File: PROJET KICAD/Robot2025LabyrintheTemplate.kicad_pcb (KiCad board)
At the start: 2 copper layers, 76.2 x 54.6 mm, 23 parts, among them J1 HC-SR04 gauche, J10 CAPTEUR TOF _BAS, J11 SERVO MOTEUR 4, J2 +VBatt, J3 SERVO MOTEUR 1, J4 SERVO MOTEUR 2, J5 cap sen0101, J7 SERVO MOTEUR 3, J8 HC-SR04 droite, J9 CAPTEUR TOF_HAUT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

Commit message: revue avec alaime
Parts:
- removed U3: NRF24L01P-Module-E01ML01DP5_Breakout, ISI-Modules:E01-ML01DP5
- added C3: C_Gen, ISI-Capacitor:C_1206_3216Metric_Pad1.33x1.80mm_HandSolder, F.Cu at (207.4, 138.0)
- added C4: C_Polarized, ISI-Capacitor:CP_EIA-6032-28_Kemet-C_Pad2.25x2.35mm_HandSolder, F.Cu at (272.9, 134.0)
- added J10: CAPTEUR TOF _BAS, ISI-Connector_PinHeader_2.54mm:PinHeader_1x06_P2.54mm_Long_Vertical, F.Cu at (209.3, 73.5)
- added J12: Conn_01x06_Pin, ISI-Connector_PinHeader_2.54mm:PinHeader_1x06_P2.54mm_Long_Vertical, F.Cu at (82.1, 34.5)
- added J13: Conn_01x06_Pin, ISI-Connector_PinHeader_2.54mm:PinHeader_1x06_P2.54mm_Long_Vertical, F.Cu at (212.9, 59.0)
- added J14: Conn_01x06_Pin, ISI-Connector_PinHeader_2.54mm:PinHeader_1x06_P2.54mm_Long_Vertical, F.Cu at (219.5, 129.4)
- added J14: Conn_01x02_Pin, ISI-Connector_JST:JST_XH_B2B-XH-AM_1x02_P2.50mm_Long_Vertical, F.Cu at (246.0, 116.0)
- added J15: CON 1x2 POLARIZED, ISI-Connector_Generic:AMASS_XT60-F_1x02_P7.20mm_Vertical, F.Cu at (64.4, 76.5)
- added J16: regulateur, ISI-Connector_JST:JST_XH_B2B-XH-AM_1x02_P2.50mm_Long_Vertical, F.Cu at (262.5, 127.2)
- added J17: Conn_01x04_Pin, ISI-Connector_JST:JST_XH_B4B-XH-AM_1x04_P2.50mm_Long_Vertical, F.Cu at (271.9, 119.4)
- added J18: Conn_01x02_Pin, ISI-Connector_JST:JST_XH_B2B-XH-AM_1x02_P2.50mm_Long_Vertical, F.Cu at (262.5, 135.0)
- added J19: Conn_01x04_Pin, ISI-Connector_JST:JST_XH_B4B-XH-AM_1x04_P2.50mm_Long_Vertical, F.Cu at (271.9, 127.2)
- added J6: Conn_01x06_Pin, ISI-Connector_PinHeader_2.54mm:PinHeader_1x06_P2.54mm_Long_Vertical, F.Cu at (83.1, 121.5)
- added J9: CAPTEUR TOF_HAUT, ISI-Connector_PinHeader_2.54mm:PinHeader_1x06_P2.54mm_Long_Vertical, F.Cu at (212.4, 99.5)
- added U2: LM1117MPX-3.3, ISI-IC:SOT-223-3_TabPin2, F.Cu at (173.2, 132.5)
- added U4: NRF24L01P-Module-E01ML01DP5_Breakout, ISI-Modules:E01-ML01DP5, F.Cu at (181.2, 145.1)
- C1, C2: value 10uF -> C_Gen; footprint ISI-Capacitor:WCAP-ATUL_18X35.5_DXL_ -> ISI-Capacitor:C_1206_3216Metric_Pad1.33x1.80mm_HandSolder
- moved U1 230.5 mm to (232.0, 85.2)
- moved A5 176.2 mm to (215.9, 122.5), turned to 90 degrees
- moved A4 176.0 mm to (210.9, 49.7), turned to 90 degrees
- moved J3 141.9 mm to (153.5, 32.0)
- moved J5 116.8 mm to (150.5, 148.0)
- moved A2 110.6 mm to (94.5, 121.5)
- moved C1 108.7 mm to (168.9, 123.0)
- moved C2 104.2 mm to (165.0, 140.5), turned to 180 degrees
- moved J10 102.2 mm to (134.9, 125.2)
- moved J11 102.2 mm to (125.6, 125.2)
- moved J4 102.2 mm to (116.3, 125.2)
- moved J7 102.2 mm to (120.9, 125.2)
- moved J8 102.2 mm to (140.7, 126.3)
- moved J9 102.2 mm to (130.2, 125.2)
- moved J2 95.7 mm to (91.2, 144.0), turned to 0 degrees
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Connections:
- A1 pad 3: unconnected-(A1-A2-Pad3) -> Net-(A1-A2)
- A1 pad 4: unconnected-(A1-A1-Pad4) -> Net-(A1-A1)
- A1 pad 5: unconnected-(A1-B1-Pad5) -> Net-(A1-B1)
- A1 pad 6: unconnected-(A1-B2-Pad6) -> Net-(A1-B2)
- A1 pad 7: unconnected-(A1-GND-Pad7) -> Net-(J12-Pin_6)
- A1 pad 8: unconnected-(A1-VMOT-Pad8) -> Net-(A1-VMOT)
- A2 pad 3V3: +3V3 -> unconnected-(A2-3.3V-Pad3V3)
- A2 pad D20: /T_SDA -> Net-(A2-D20/SDA)
- A2 pad D21: /T_SCL -> Net-(A2-D21/SCL)
- A2 pad SCL: /SCL_1 -> unconnected-(A2-PadSCL)
- A2 pad SDA: /SDA_1 -> unconnected-(A2-PadSDA)
- A2 pad VIN: /Vin -> unconnected-(A2-PadVIN)
- A3 pad 3: unconnected-(A3-A2-Pad3) -> Net-(A3-A2)
- A3 pad 4: unconnected-(A3-A1-Pad4) -> Net-(A3-A1)
- A3 pad 5: unconnected-(A3-B1-Pad5) -> Net-(A3-B1)
- A3 pad 6: unconnected-(A3-B2-Pad6) -> Net-(A3-B2)
- A3 pad 7: unconnected-(A3-GND-Pad7) -> Net-(J6-Pin_6)
- A3 pad 8: unconnected-(A3-VMOT-Pad8) -> Net-(A3-VMOT)
- A4 pad 3: unconnected-(A4-A2-Pad3) -> Net-(A4-A2)
- A4 pad 4: unconnected-(A4-A1-Pad4) -> Net-(A4-A1)
- A5 pad 3: unconnected-(A5-A2-Pad3) -> Net-(A5-A2)
- A5 pad 4: unconnected-(A5-A1-Pad4) -> Net-(A5-A1)
- A5 pad 5: unconnected-(A5-B1-Pad5) -> Net-(A5-B1)
- A5 pad 6: unconnected-(A5-B2-Pad6) -> Net-(A5-B2)
- A5 pad 7: unconnected-(A5-GND-Pad7) -> GND
- A5 pad 8: unconnected-(A5-VMOT-Pad8) -> /Vin
- C1 pad 1: +3V3 -> Net-(U2-VO)
- C2 pad 1: GND -> +5V
- U1 pad 3: /SCL_1 -> Net-(A2-D21/SCL)
- U1 pad 4: /SDA_1 -> Net-(A2-D20/SDA)
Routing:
- net (no net): track 286.5 -> 0.00 mm, vias 4 -> 0
- net +3V3: track 29.8 -> 0.00 mm, vias 1 -> 0
- net /Trig_G: track 16.4 -> 0.00 mm, vias 1 -> 0
- net /Echo_G: track 15.8 -> 0.00 mm
- net /Vin: track 14.5 -> 0.00 mm
- net Net-(D3-A): track 5.55 -> 0.00 mm
- net Net-(D3-K): track 5.52 -> 0.00 mm
- net Net-(D2-A): track 2.40 -> 0.00 mm
- net GND: track 1.90 -> 0.00 mm, vias 1 -> 0
- removed copper zone on F.Cu, net +5V
- removed copper zone on B.Cu, net GND
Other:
- board size 76.2 x 54.6 mm -> 215 x 90 mm
- board text removed: "+"
- board text removed: "-"
- board text removed: "Capteur Temp"
- board text removed: "HC-SR04"
- board text removed: "Power"
- board text removed: "Projet B3 labyrinthe 2025"
- board text removed: "RFID-RC522"
- board text removed: "Servomoteur N1"
- board text removed: "Sig"

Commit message: test2
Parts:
- moved U1 55.5 mm to (183.0, 59.3)
- moved J3 8.11 mm to (148.0, 37.9)
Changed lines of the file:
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@@
 	(footprint "ISI-Connector_PinHeader_2.54mm:PinHeader_1x03_P2.54mm_Long_Vertical"
 		(layer "F.Cu")
-		(at 153.5 31.96)
+		(at 148 37.92)
 		(descr "Through hole straight pin header, 1x03, 2.54mm pitch, single row")
 		(tags "Through hole pin header THT 1x03 2.54mm single row")
@@
 	(footprint "ISI-Modules:module_mpu6050"
 		(layer "F.Cu")
-		(at 232 85.24)
+		(at 183 59.28)
 		(descr "Module 6 DoF I2C basé sur un MPU6050 associant un accéléromètre 3 axes et un gyroscope 3 axes.")
 		(property "Reference" "U1"

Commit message: fin de la schematique, debut rotage
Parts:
- removed C3: C_Gen, ISI-Capacitor:C_1206_3216Metric_Pad1.33x1.80mm_HandSolder
- removed J10 (x2): CAPTEUR TOF _BAS, ISI-Connector_PinHeader_2.54mm:PinHeader_1x06_P2.54mm_Long_Vertical
- removed J12: Conn_01x06_Pin, ISI-Connector_PinHeader_2.54mm:PinHeader_1x06_P2.54mm_Long_Vertical
- removed the J14 at (219.5, 129.4)
- removed J19: Conn_01x04_Pin, ISI-Connector_JST:JST_XH_B4B-XH-AM_1x04_P2.50mm_Long_Vertical
- removed J5: cap sen0101, ISI-Connector_PinSocket_2.54mm:PinSocket_2x04_P2.54mm_Vertical
- removed J9 (x2): CAPTEUR TOF_HAUT, ISI-Connector_PinHeader_2.54mm:PinHeader_1x06_P2.54mm_Long_Vertical
- added F1: Fuse, ISI-Divers:Fuseholder_TR5_Littelfuse_No560_No460, F.Cu at (59.5, 88.0)
- added J20: moteur 3 DR, ISI-Connector_JST:JST_XH_B4B-XH-AM_1x04_P2.50mm_Long_Vertical, F.Cu at (61.5, 58.0)
- added J21: moteur 4 DR, ISI-Connector_JST:JST_XH_B4B-XH-AM_1x04_P2.50mm_Long_Vertical, F.Cu at (56.5, 127.0)
- added J22: moteur 1 AV, ISI-Connector_JST:JST_XH_B4B-XH-AM_1x04_P2.50mm_Long_Vertical, F.Cu at (228.0, 74.0)
- added R2: 10k, ISI-Resistor:R_1206_3216Metric_Pad1.30x1.75mm_HandSolder, F.Cu at (181.4, 56.5)
- added R3: 10k, ISI-Resistor:R_1206_3216Metric_Pad1.30x1.75mm_HandSolder, F.Cu at (181.9, 60.5)
- J13: value Conn_01x06_Pin -> capteur TOF BAS; footprint ISI-Connector_PinHeader_2.54mm:PinHeader_1x06_P2.54mm_Long_Vertical -> ISI-Connector_JST:JST_XH_B5B-XH-AM_1x05_P2.50mm_Long_Vertical
- J14: value Conn_01x02_Pin -> Vinput regul
- J16: value regulateur -> capteur TOF HAUT; footprint ISI-Connector_JST:JST_XH_B2B-XH-AM_1x02_P2.50mm_Long_Vertical -> ISI-Connector_JST:JST_XH_B5B-XH-AM_1x05_P2.50mm_Long_Vertical
- J17: value Conn_01x04_Pin -> moteur 2 AV
- J18: value Conn_01x02_Pin -> Vout regul
- J2: value +VBatt -> cap sen0101; footprint ISI-Connector_JST:JST_XH_B2B-XH-AM_1x02_P2.50mm_Long_Vertical -> ISI-Connector_JST:JST_XH_B4B-XH-AM_1x04_P2.50mm_Long_Vertical; moved to B.Cu
- J6: value Conn_01x06_Pin -> cap sen0101; footprint ISI-Connector_PinHeader_2.54mm:PinHeader_1x06_P2.54mm_Long_Vertical -> ISI-Connector_JST:JST_XH_B4B-XH-AM_1x04_P2.50mm_Long_Vertical; moved to B.Cu
- moved J18 157.7 mm to (105.0, 126.0)
- moved J14 153.3 mm to (93.0, 125.5)
- moved J4 106.3 mm to (222.5, 122.5)
- moved J2 86.7 mm to (119.5, 62.0), turned to 90 degrees
- moved J7 86.2 mm to (71.0, 54.9)
- moved S1 73.9 mm to (73.0, 89.5)
- moved J3 69.5 mm to (215.0, 56.5)
- moved D3 65.8 mm to (63.3, 97.5)
- moved J6 64.8 mm to (107.5, 61.5), turned to 90 degrees
- moved C4 62.0 mm to (211.6, 125.0)
- moved R1 59.2 mm to (71.0, 93.5)
- moved J11 51.1 mm to (74.5, 124.0)
- moved J16 47.8 mm to (228.0, 94.0)
- moved C2 46.8 mm to (211.0, 132.0)
- moved D2 46.8 mm to (74.0, 98.0)
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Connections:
- A1 pad 10: +5V -> GND
- A1 pad 11: +5V -> GND
- A1 pad 12: +5V -> GND
- A1 pad 7: Net-(J12-Pin_6) -> GND
- A1 pad 8: Net-(A1-VMOT) -> /Vin
- A3 pad 10: +5V -> GND
- A3 pad 11: +5V -> GND
- A3 pad 12: +5V -> GND
- A3 pad 7: Net-(J6-Pin_6) -> GND
- A3 pad 8: Net-(A3-VMOT) -> /Vin
- A4 pad 10: +5V -> GND
- A4 pad 11: +5V -> GND
- A4 pad 12: +5V -> GND
- A4 pad 5: unconnected-(A4-B1-Pad5) -> Net-(A4-B1)
- A4 pad 6: unconnected-(A4-B2-Pad6) -> Net-(A4-B2)
- A4 pad 7: unconnected-(A4-GND-Pad7) -> GND
- A4 pad 8: unconnected-(A4-VMOT-Pad8) -> /Vin
- J11 pad 2: unconnected-(J11-Pin_2-Pad2) -> +5V
- J13 pad 1: Net-(A4-VMOT) -> +5V
- J13 pad 2: Net-(A4-A1) -> GND
- J13 pad 3: Net-(A4-A2) -> Net-(A2-D21/SCL)
- J13 pad 4: Net-(A4-B1) -> Net-(A2-D20/SDA)
- J13 pad 5: Net-(A4-B2) -> /D_XSHUT_B
- J14 pad 1: unconnected-(J14-Pin_1-Pad1) -> /Vin
- J14 pad 2: unconnected-(J14-Pin_2-Pad2) -> GND
- J15 pad 1: unconnected-(J15-Pad1) -> Net-(F1-Pad1)
- J15 pad 2: unconnected-(J15-Pad2) -> GND
- J16 pad 1: unconnected-(J16-Pin_1-Pad1) -> +5V
- J16 pad 2: unconnected-(J16-Pin_2-Pad2) -> GND
- J17 pad 1: Net-(A5-B2) -> Net-(A5-A1)
- J17 pad 2: Net-(A5-B1) -> Net-(A5-A2)
- J17 pad 3: Net-(A5-A2) -> Net-(A5-B1)
- J17 pad 4: Net-(A5-A1) -> Net-(A5-B2)
- J2 pad 1: Net-(D3-A) -> GND
- J2 pad 2: GND -> /D_OUT
- J3 pad 2: unconnected-(J3-Pin_2-Pad2) -> +5V
- J4 pad 2: unconnected-(J4-Pin_2-Pad2) -> +5V
- J6 pad 1: Net-(A3-VMOT) -> /D_S0
- J6 pad 2: Net-(A3-A1) -> /D_S1
- J6 pad 3: Net-(A3-A2) -> /D_S2
- J6 pad 4: Net-(A3-B1) -> /D_S3
- J7 pad 2: unconnected-(J7-Pin_2-Pad2) -> +5V
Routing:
- net Net-(A2-D21/SCL): track 0.00 -> 37.6 mm
- net Net-(A1-A2): track 0.00 -> 24.6 mm
- net Net-(A3-A2): track 0.00 -> 23.5 mm
- net Net-(A5-A2): track 0.00 -> 22.7 mm
- net Net-(A4-A2): track 0.00 -> 21.4 mm
- net Net-(A2-D20/SDA): track 0.00 -> 16.9 mm
- net Net-(A3-B1): track 0.00 -> 12.1 mm
- net Net-(A3-B2): track 0.00 -> 12.1 mm
- net Net-(A3-A1): track 0.00 -> 11.1 mm
- net Net-(A1-A1): track 0.00 -> 9.18 mm
- net Net-(A5-B1): track 0.00 -> 8.98 mm
- net Net-(A5-B2): track 0.00 -> 8.96 mm
- net Net-(A1-B2): track 0.00 -> 8.17 mm
- net Net-(A1-B1): track 0.00 -> 8.16 mm
- net Net-(A5-A1): track 0.00 -> 7.96 mm
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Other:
- board size 215 x 90 mm -> 210 x 85 mm

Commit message: routage 1
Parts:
- moved U1 85.3 mm to (123.0, 76.0), turned to -90 degrees
- moved J8 38.5 mm to (161.5, 88.0)
- moved J18 31.8 mm to (109.5, 94.5)
- moved J14 31.3 mm to (97.5, 94.5)
- moved J1 13.0 mm to (161.5, 101.5)
- moved S1 11.6 mm to (84.5, 89.0)
- moved R1 11.0 mm to (82.0, 93.0)
- moved D2 9.51 mm to (83.5, 97.5)
- moved D3 9.00 mm to (72.3, 97.5)
- moved C4 8.16 mm to (204.8, 120.3)
- moved C1 8.16 mm to (204.8, 114.3)
- moved C2 8.16 mm to (204.3, 127.3)
- moved F1 7.57 mm to (66.9, 89.5)
- moved U2 7.29 mm to (196.0, 120.7)
- moved U4 5.06 mm to (192.3, 110.0)
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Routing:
- net Net-(A2-D21/SCL): track 37.6 -> 16.2 mm
- net Net-(A2-D20/SDA): track 16.9 -> 19.1 mm
- net Net-(A3-A1): track 11.1 -> 9.76 mm

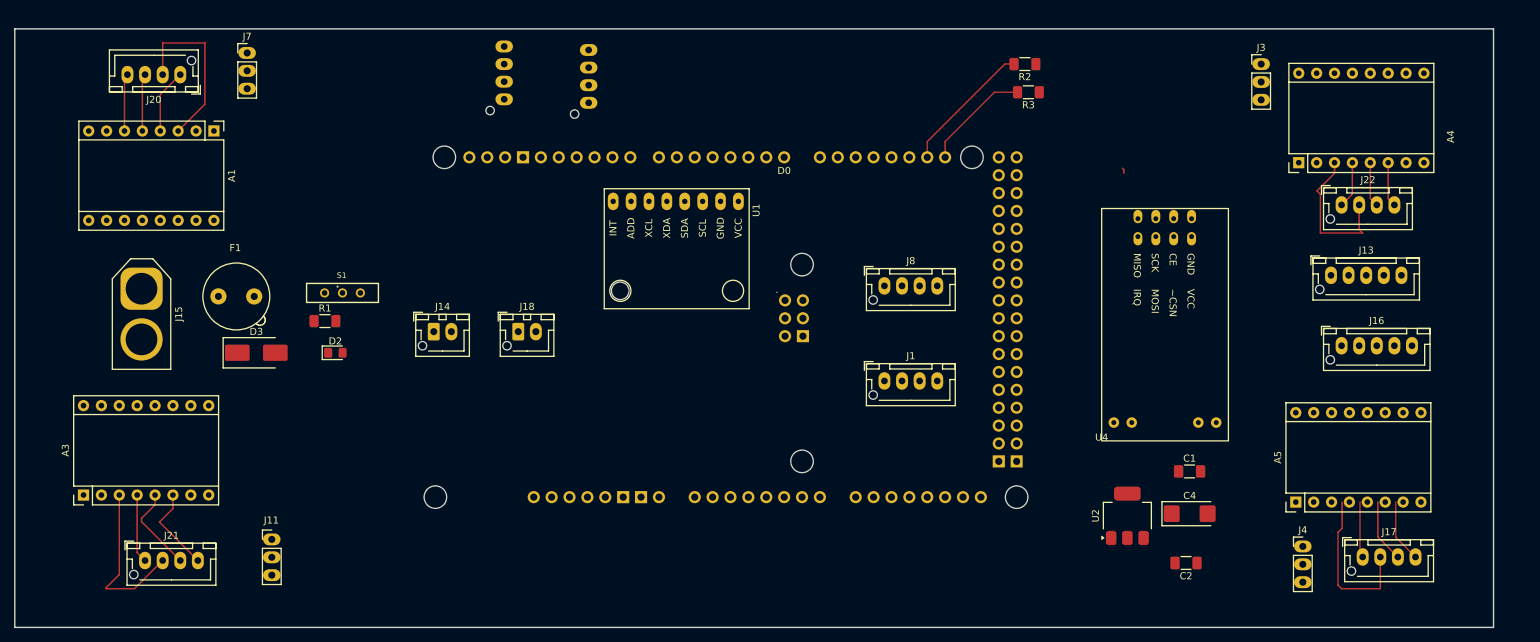
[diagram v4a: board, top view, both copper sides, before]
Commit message: gnd et 5v
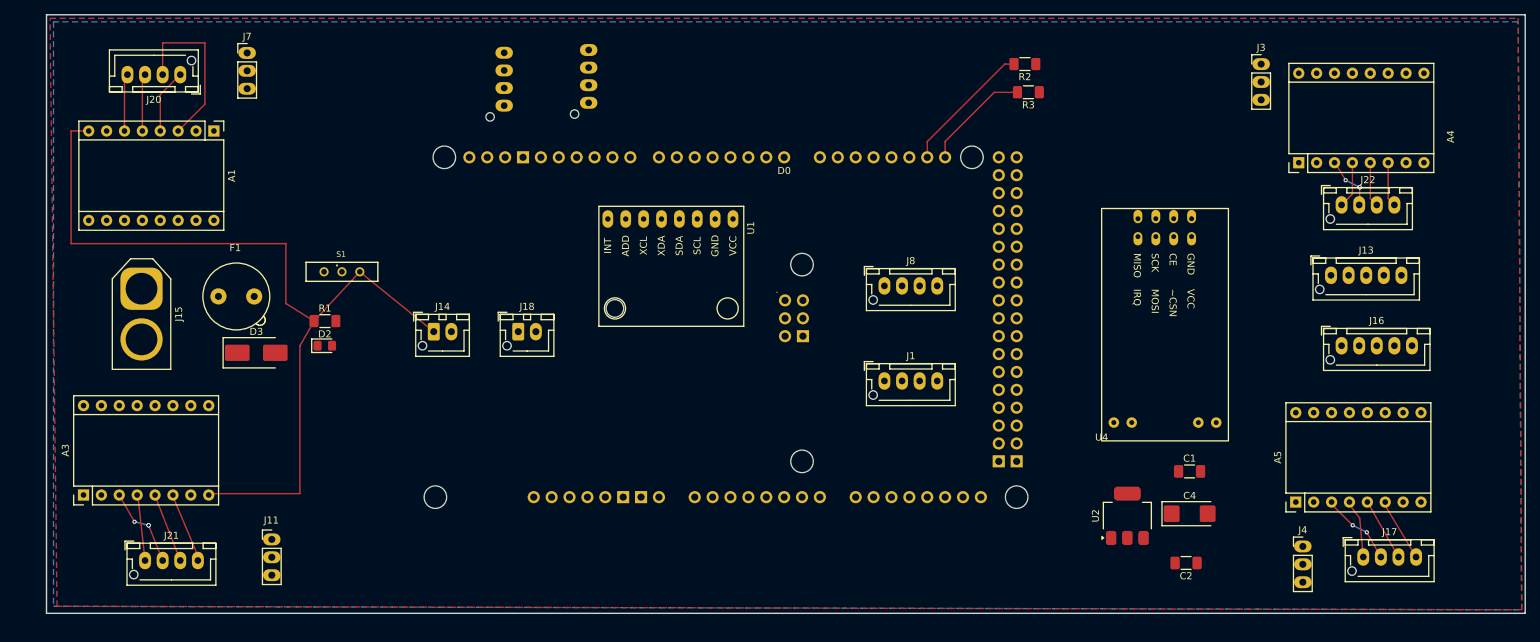
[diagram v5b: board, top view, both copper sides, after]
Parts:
- moved S1 3.00 mm to (84.5, 86.0)
- moved U1 2.61 mm to (122.2, 78.5)
- moved D2 1.80 mm to (82.0, 96.5)
- moved J6 0.90 mm to (107.5, 62.4)
- moved J17 0.08 mm to (229.5, 126.5)
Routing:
- net Net-(A3-A2): track 23.8 -> 0.00 mm, vias 0 -> 3
- net Net-(A5-A2): track 22.7 -> 0.00 mm, vias 0 -> 2
- net Net-(A4-A2): track 21.4 -> 0.00 mm, vias 0 -> 3
- net Net-(A3-B1): track 12.4 -> 0.00 mm
- net Net-(A3-B2): track 12.4 -> 0.00 mm
- net Net-(A3-A1): track 9.76 -> 0.00 mm
- net Net-(A5-B1): track 8.98 -> 0.00 mm
- net Net-(A5-B2): track 8.96 -> 0.00 mm
- net Net-(A5-A1): track 7.96 -> 0.54 mm
- net Net-(A2-D21/SCL): track 16.2 -> 15.4 mm
- added copper zone on F.Cu, net +5V
- added copper zone on B.Cu, net GND

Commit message: maj2
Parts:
- moved S1 14.8 mm to (77.5, 73.0)
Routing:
- net /Vin: track 0.00 -> 288.4 mm, vias 0 -> 10
- net /wht_2: track 0.00 -> 242.0 mm, vias 0 -> 2
- net /d2-DIR: track 0.00 -> 178.3 mm, vias 0 -> 2
- net Net-(A2-D20/SDA): track 19.1 -> 177.8 mm, vias 0 -> 2
- net /d2-STEP: track 0.00 -> 142.2 mm, vias 0 -> 2
- net /d1-ENABLE: track 0.00 -> 137.4 mm
- net /d2-ENABLE: track 0.00 -> 121.9 mm, vias 0 -> 2
- net Net-(A2-D21/SCL): track 15.4 -> 133.2 mm, vias 0 -> 4
- net /d1-DIR: track 0.00 -> 116.6 mm
- net /d1-STEP: track 0.00 -> 116.6 mm
- net /d3-ENABLE: track 0.00 -> 106.1 mm
- net +5V: track 0.00 -> 97.8 mm, vias 0 -> 5
- net /wht_4: track 0.00 -> 95.1 mm, vias 0 -> 2
- net /wht_1: track 0.00 -> 90.6 mm, vias 0 -> 2
- net /wht_3: track 0.00 -> 79.4 mm, vias 0 -> 2
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
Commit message: next
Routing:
- net +5V: track 97.8 -> 97.1 mm
- net /D_CE: track 44.6 -> 45.1 mm
